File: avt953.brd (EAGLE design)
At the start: 100 x 80 mm, 51 parts, among them CON3 RJ45-6L2-B, CON4A MKDS_5/3-6,35, CON4B MKDS_5/3-6,35, CON4C MKDS_5/3-6,35, CON4D MKDS_5/3-6,35, X1 20MHz, X2 20MHz

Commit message: Wstępnie rozmieszczono wszystkie elementy na projekcie płytki PCB.
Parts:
- C1, C3: device resistor:E5-13 -> resistor:TT2D5
- moved R5 299.4 mm to (72.4, 76.2)
- moved R4 285.2 mm to (53.3, 72.4), turned to 90 degrees
- moved C21 274.0 mm to (53.3, 67.3), turned to 270 degrees
- moved R3 269.6 mm to (43.2, 71.1), flipped to the bottom, turned to 270 degrees
- moved R2 255.4 mm to (80.0, 15.2), turned to 90 degrees
- moved C6 241.2 mm to (30.5, 71.1), flipped to the bottom, turned to 90 degrees
- moved D2 239.0 mm to (78.7, 5.08)
- moved C5 238.3 mm to (63.5, 40.6), flipped to the bottom, turned to 90 degrees
- moved C4 238.3 mm to (63.5, 45.7), flipped to the bottom, turned to 270 degrees
- moved C7 235.8 mm to (27.9, 71.1), flipped to the bottom, turned to 90 degrees
- moved LED 233.2 mm to (16.5, 76.2), turned to 180 degrees
- moved X1 229.0 mm to (68.6, 43.2), flipped to the bottom, turned to 90 degrees
- moved D3 180.2 mm to (39.4, 31.8), flipped to the bottom, turned to 90 degrees
- moved R9 176.6 mm to (26.7, 24.1), flipped to the bottom, turned to 180 degrees
- moved D5 173.4 mm to (36.8, 31.8), flipped to the bottom, turned to 90 degrees
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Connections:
- removed net VDD3: US5.47
- net VCC: now also US5.47

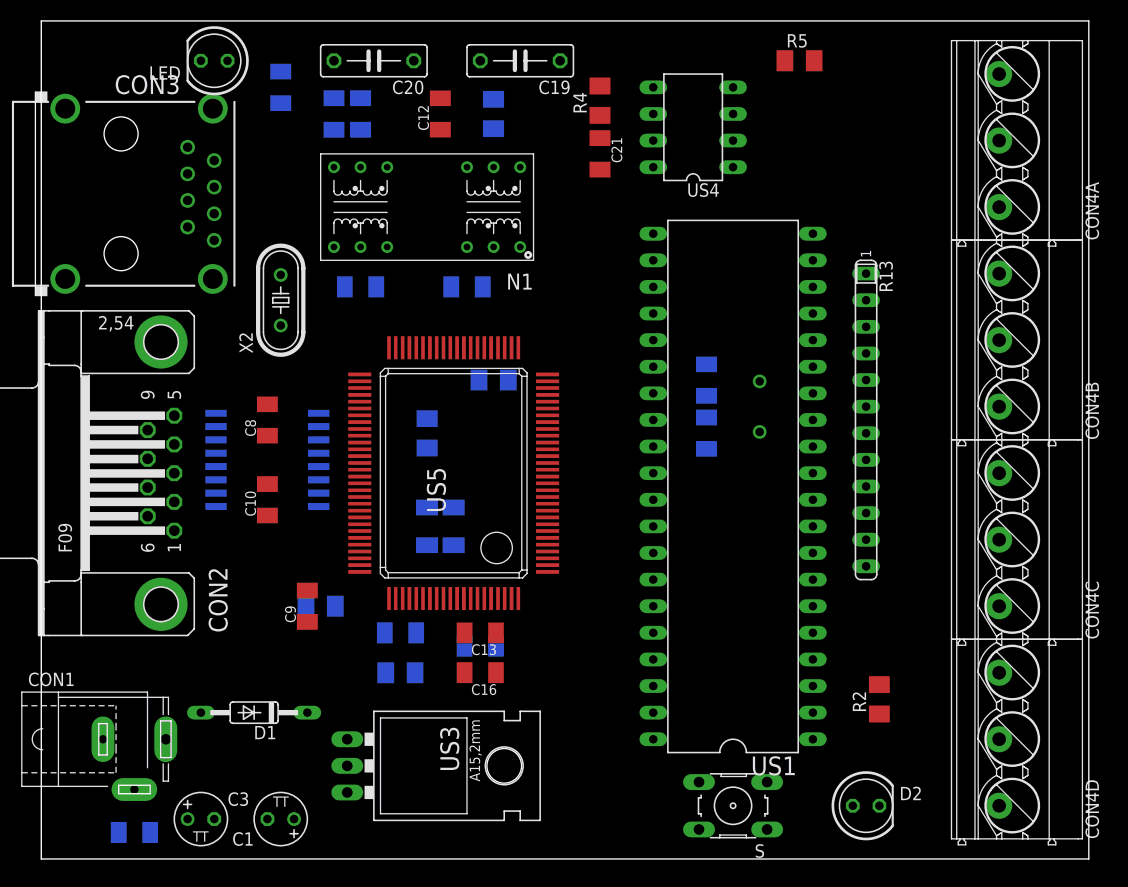
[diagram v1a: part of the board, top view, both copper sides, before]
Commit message: Dodano otwory montażowe M3 w rogach płytki.
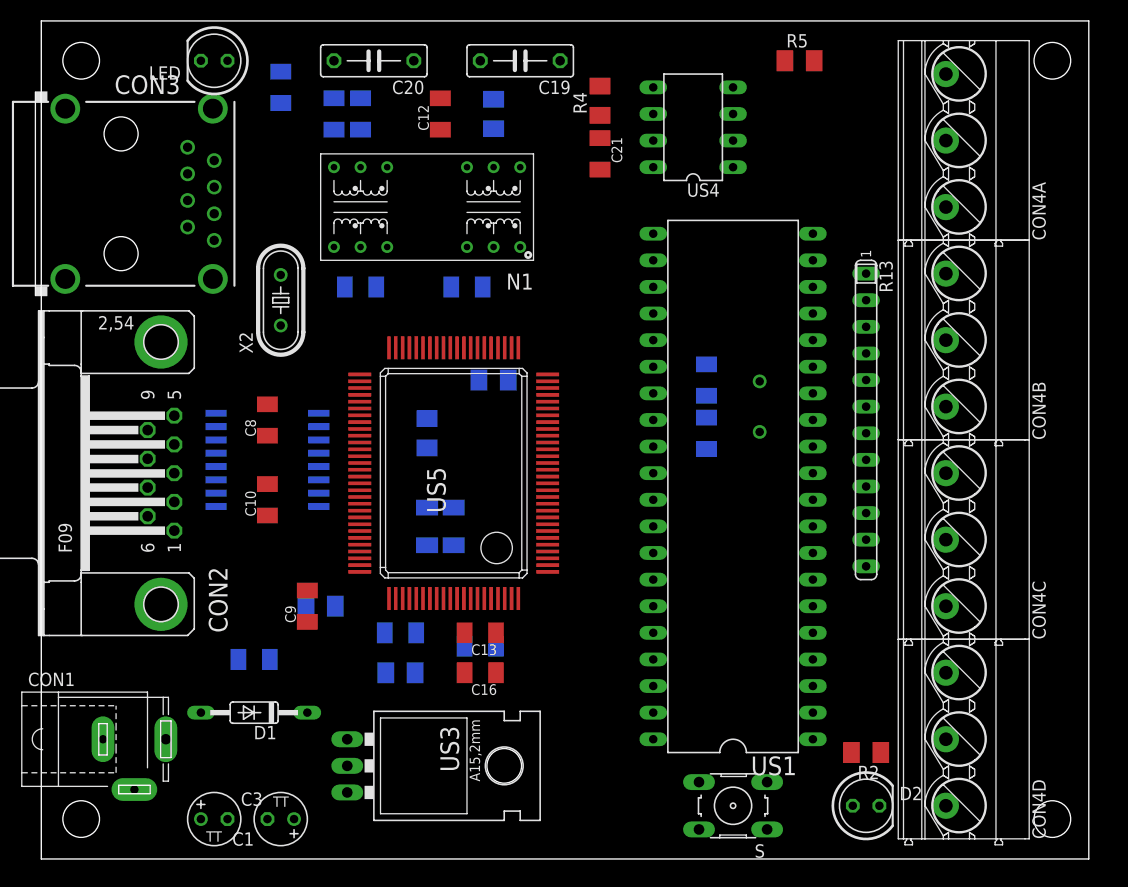
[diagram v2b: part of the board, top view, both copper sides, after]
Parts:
- moved C2 20.1 mm to (20.3, 19.1)
- moved R2 5.24 mm to (78.7, 10.2), turned to 180 degrees
- moved CON4A 5.08 mm to (86.4, 68.6)
- moved CON4B 5.08 mm to (86.4, 49.5)
- moved CON4C 5.08 mm to (86.4, 30.5)
- moved CON4D 5.08 mm to (86.4, 11.4)
- moved C3 1.27 mm to (16.5, 3.81)

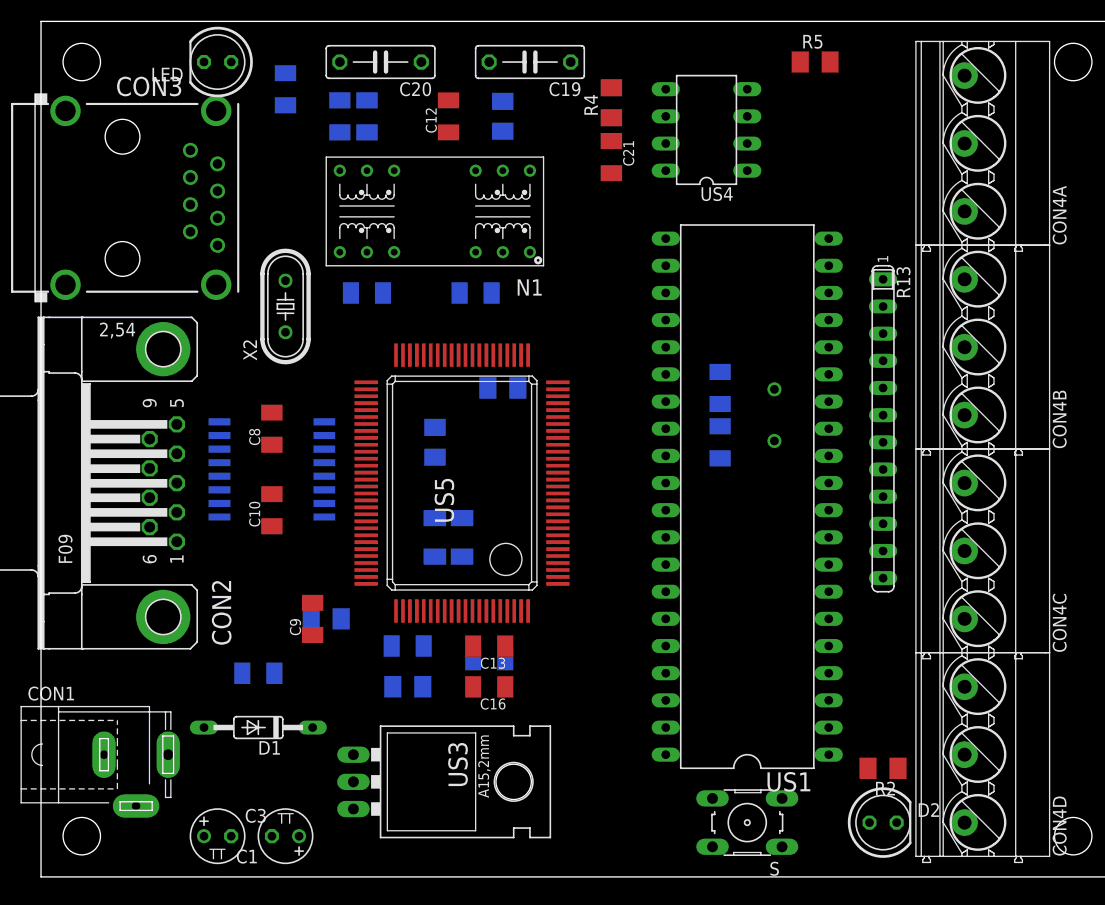
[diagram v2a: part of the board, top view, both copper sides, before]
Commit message: Przepuszczono płytkę przez autorouter z wynikiem 72,6%.
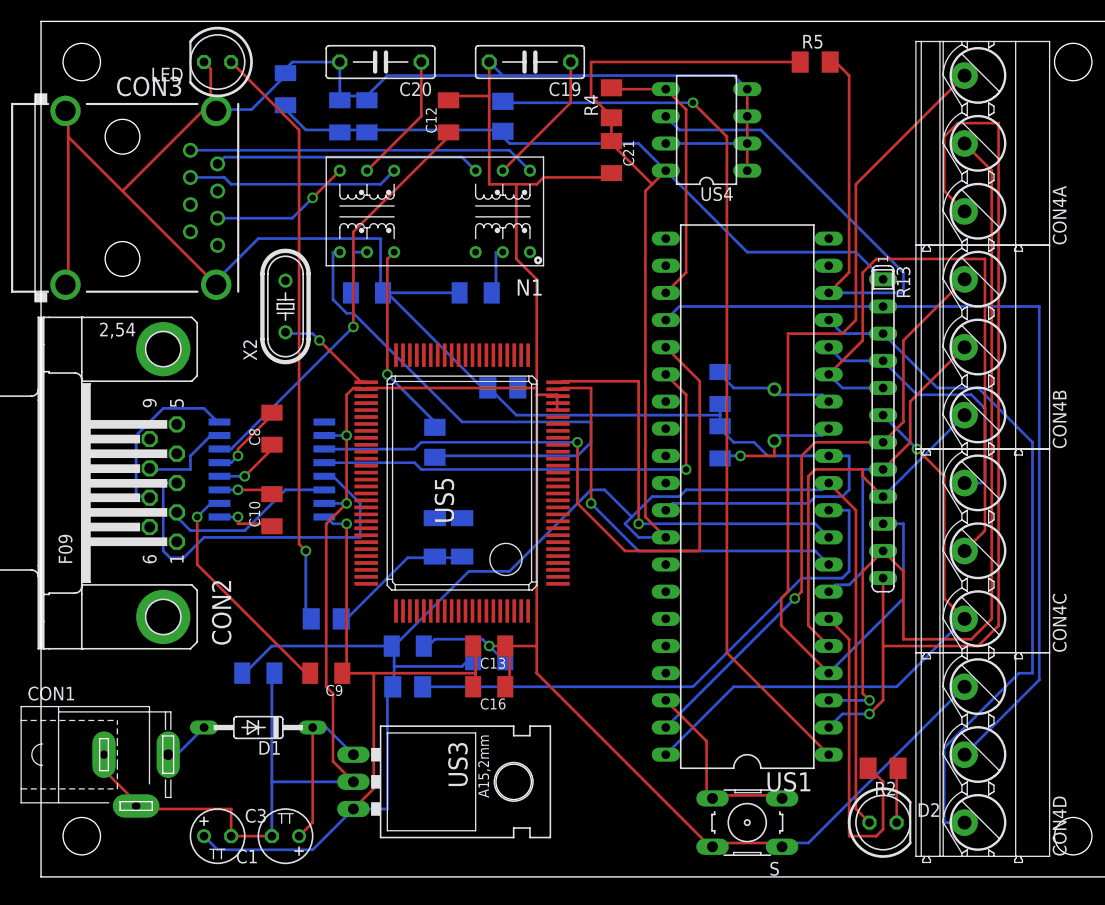
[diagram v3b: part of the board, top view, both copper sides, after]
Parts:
- moved C9 5.24 mm to (26.7, 19.1), turned to 180 degrees
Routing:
- net GND: track 0.00 -> 484.1 mm, vias 0 -> 3
- net VCC: track 0.00 -> 325.1 mm, vias 0 -> 1
- net IN0: track 0.00 -> 89.5 mm, vias 0 -> 1
- net IN2: track 0.00 -> 86.6 mm
- net N$35: track 0.00 -> 84.1 mm, vias 0 -> 1
- net IN1: track 0.00 -> 82.4 mm, vias 0 -> 1
- net IN10: track 0.00 -> 80.3 mm
- net IN9: track 0.00 -> 65.4 mm
- net TXD: track 0.00 -> 63.3 mm, vias 0 -> 1
- net N$37: track 0.00 -> 60.6 mm
- net IN5: track 0.00 -> 57.2 mm, vias 0 -> 1
- net IN7: track 0.00 -> 56.5 mm
- net N$31: track 0.00 -> 55.5 mm, vias 0 -> 1
- net IN6: track 0.00 -> 55.4 mm, vias 0 -> 1
- net RESET: track 0.00 -> 52.0 mm
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
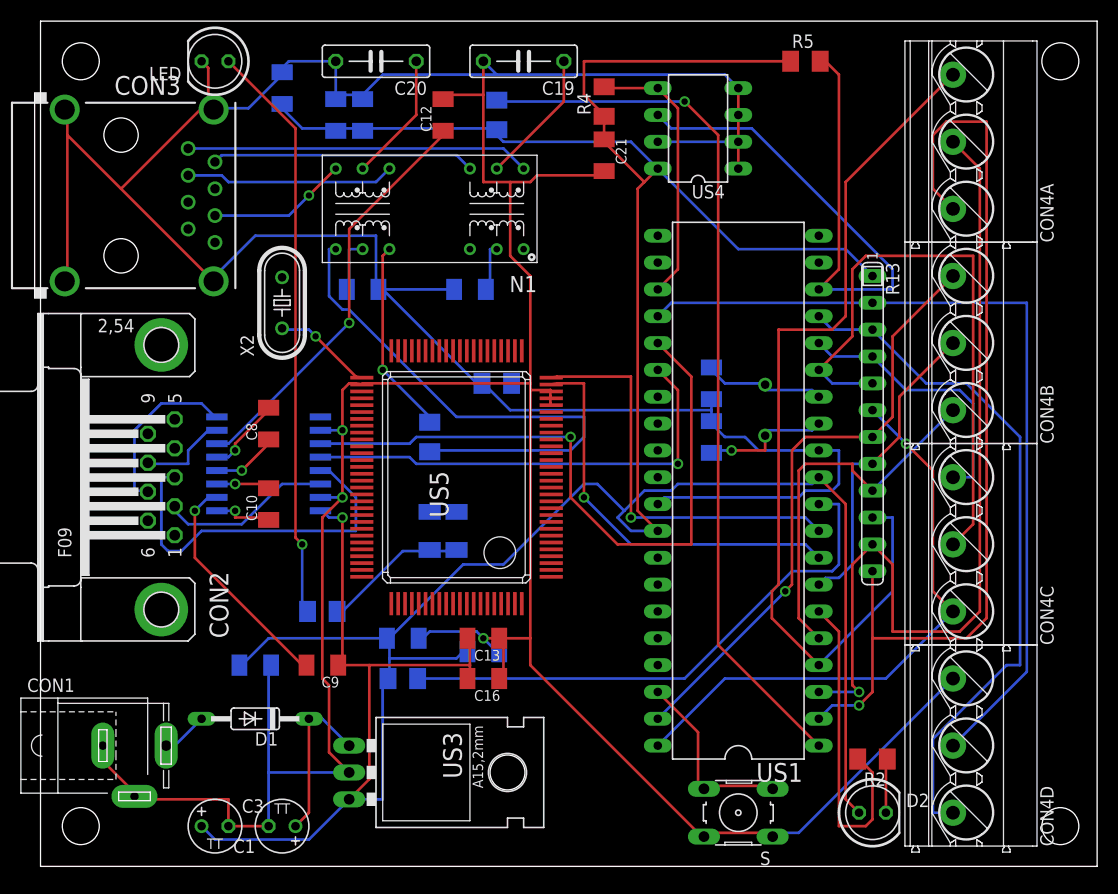
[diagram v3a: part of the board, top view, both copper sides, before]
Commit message: Cofnięcie autoroutera. Zmiana kolejności wyprowadzeń IN (bo pin GND) nie był zewnętrznym pinem.
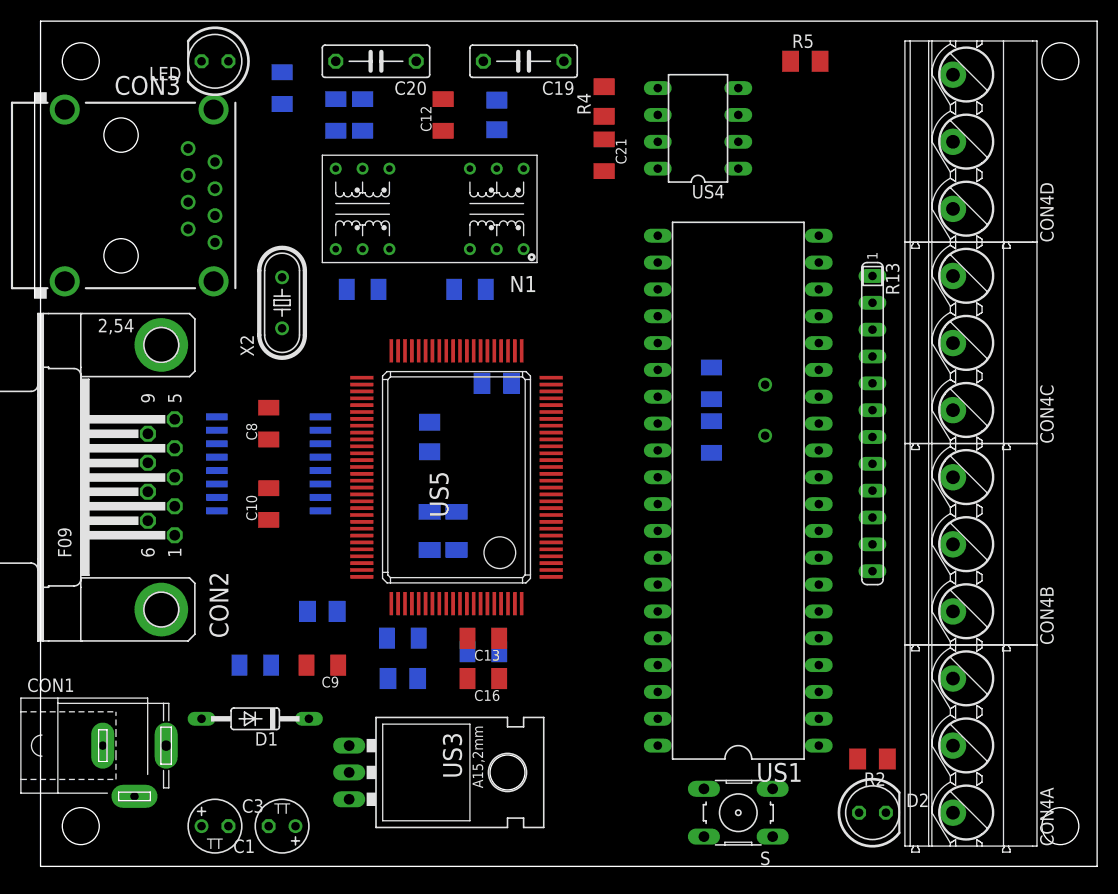
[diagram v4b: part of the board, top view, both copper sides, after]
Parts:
- moved CON4A 57.1 mm to (86.4, 11.4)
- moved CON4D 57.1 mm to (86.4, 68.6)
- moved CON4B 19.1 mm to (86.4, 30.5)
- moved CON4C 19.1 mm to (86.4, 49.5)
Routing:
- net GND: track 484.1 -> 0.00 mm, vias 3 -> 0
- net VCC: track 325.1 -> 0.00 mm, vias 1 -> 0
- net IN0: track 89.5 -> 0.00 mm, vias 1 -> 0
- net IN2: track 86.6 -> 0.00 mm
- net N$35: track 84.1 -> 0.00 mm, vias 1 -> 0
- net IN1: track 82.4 -> 0.00 mm, vias 1 -> 0
- net IN10: track 80.3 -> 0.00 mm
- net IN9: track 65.4 -> 0.00 mm
- net TXD: track 63.3 -> 0.00 mm, vias 1 -> 0
- net N$37: track 60.6 -> 0.00 mm
- net IN5: track 57.2 -> 0.00 mm, vias 1 -> 0
- net IN7: track 56.5 -> 0.00 mm
- net N$31: track 55.5 -> 0.00 mm, vias 1 -> 0
- net IN6: track 55.4 -> 0.00 mm, vias 1 -> 0
- net RESET: track 52.0 -> 0.00 mm
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
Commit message: Przepuszczono płytkę jeszcze raz przez autorouter, rozluźniając kryteria dodania przelotek i zmiany kierunku ścieżek. Brzydko wyszło, ale wynik 100%.
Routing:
- net GND: track 0.00 -> 452.1 mm, vias 0 -> 10
- net VCC: track 0.00 -> 349.7 mm, vias 0 -> 10
- net RESET: track 0.00 -> 96.6 mm, vias 0 -> 4
- net N$35: track 0.00 -> 85.3 mm, vias 0 -> 5
- net RXD: track 0.00 -> 66.6 mm, vias 0 -> 5
- net N$31: track 0.00 -> 62.7 mm, vias 0 -> 2
- net TXD: track 0.00 -> 52.9 mm, vias 0 -> 5
- net IN6: track 0.00 -> 48.8 mm
- net IN5: track 0.00 -> 46.8 mm, vias 0 -> 1
- net IN10: track 0.00 -> 41.3 mm
- net N$2: track 0.00 -> 41.3 mm, vias 0 -> 1
- net SD1: track 0.00 -> 40.2 mm, vias 0 -> 3
- net N$37: track 0.00 -> 39.2 mm
- net SD0: track 0.00 -> 35.5 mm, vias 0 -> 1
- net SD3: track 0.00 -> 34.3 mm, vias 0 -> 1
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
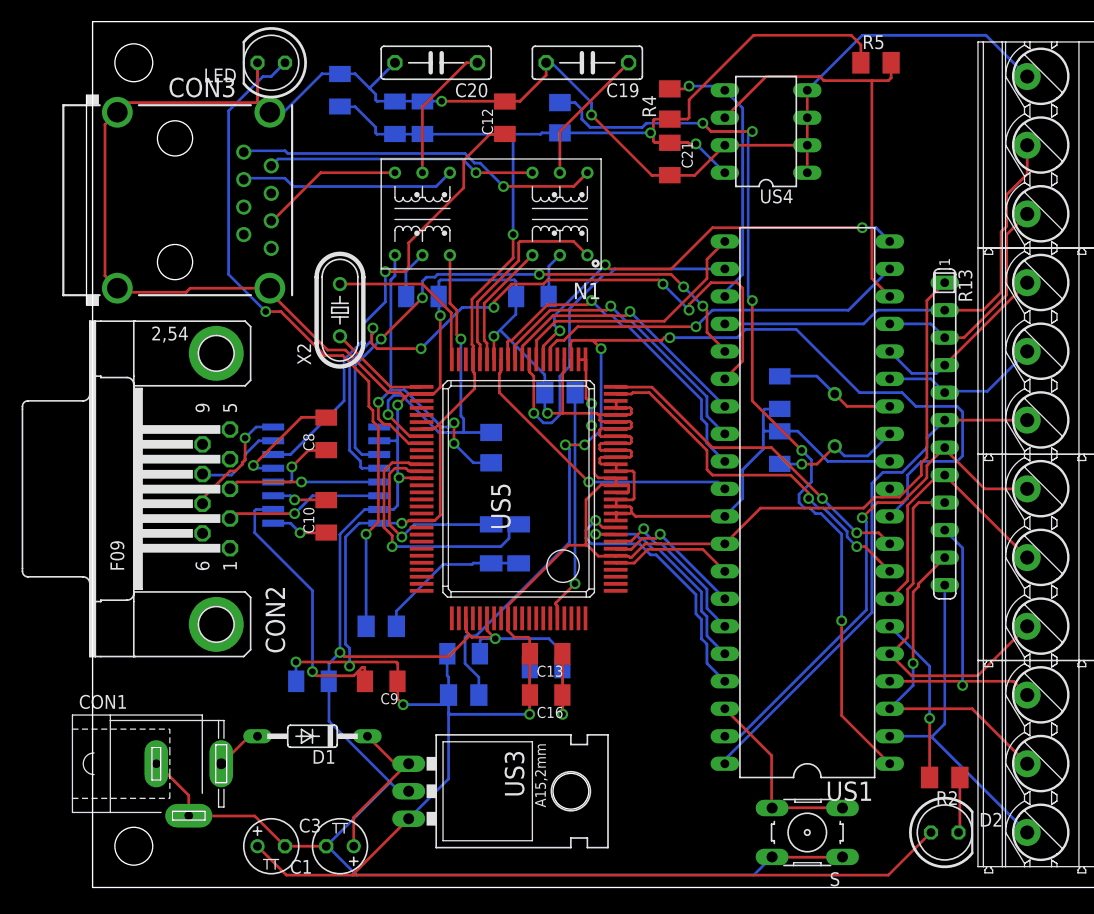
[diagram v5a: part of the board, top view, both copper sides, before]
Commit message: Poprawki po autorouterze. Usunięto sporo przelotek, a pozostałe oddalono od siebie.
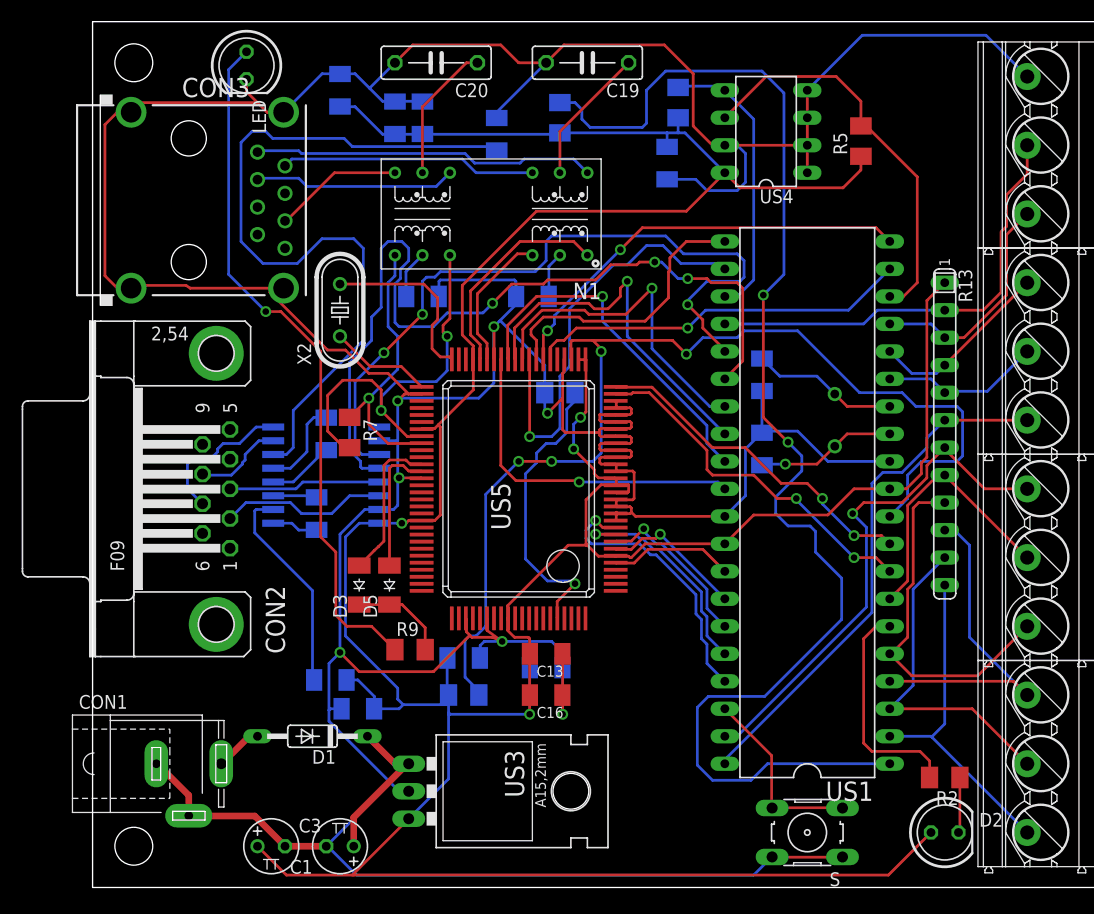
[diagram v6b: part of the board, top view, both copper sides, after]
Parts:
- moved D3 15.2 mm to (24.6, 27.9), flipped to the top
- moved R7 13.2 mm to (23.7, 42.0), flipped to the top, turned to 270 degrees
- moved D5 10.1 mm to (27.4, 27.9), flipped to the top
- moved R5 7.37 mm to (71.0, 69.0), turned to 90 degrees
- moved C2 4.90 mm to (24.5, 16.5), turned to 0 degrees
- moved C9 4.70 mm to (22.0, 19.2), flipped to the bottom, turned to 0 degrees
- moved R9 3.43 mm to (29.3, 22.0), flipped to the top, turned to 0 degrees
- moved C4 2.33 mm to (61.8, 47.4)
- moved LED 2.30 mm to (14.2, 75.9), turned to 270 degrees
- moved C12 1.70 mm to (37.3, 69.6), flipped to the bottom
- moved C5 1.66 mm to (61.8, 40.5)
- moved CON3 1.27 mm to (8.89, 63.5)
- moved C10 0.92 mm to (20.7, 34.5), flipped to the bottom
- moved R4 0.77 mm to (54.1, 72.5), flipped to the bottom
- moved C21 0.46 mm to (53.1, 66.9), flipped to the bottom
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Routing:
- net GND: track 452.1 -> 490.8 mm, vias 10 -> 7
- net N$35: track 85.3 -> 123.6 mm, vias 5 -> 2
- net N$2: track 41.3 -> 70.6 mm, vias 1 -> 0
- net TXD: track 52.9 -> 67.6 mm, vias 5 -> 3
- net RXD: track 66.6 -> 78.9 mm, vias 5 -> 3
- net N$26: track 24.4 -> 14.1 mm, vias 1 -> 0
- net N$22: track 34.2 -> 25.5 mm, vias 3 -> 1
- net SD4: track 24.9 -> 31.1 mm
- net N$29: track 18.4 -> 12.3 mm, vias 1 -> 0
- net N$1: track 25.4 -> 19.6 mm, vias 1 -> 0
- net SD5: track 28.1 -> 33.8 mm
- net N$30: track 14.6 -> 9.01 mm
- net N$27: track 21.7 -> 27.2 mm
- net N$36: track 15.5 -> 20.8 mm, vias 1 -> 0
- net SD3: track 34.3 -> 39.4 mm
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
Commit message: Dodano szablon testu DRC za https://www.allpcb.com/standard_pcb_manufacturing_capability.html. Poddano płytkę testowi i poprawiono drobne błędy.
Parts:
- moved C15 0.38 mm to (34.3, 20.8)
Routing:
- net GND: track 490.8 -> 442.3 mm
- net A4: track 25.6 -> 26.7 mm
- net VCC: track 351.1 -> 350.2 mm
